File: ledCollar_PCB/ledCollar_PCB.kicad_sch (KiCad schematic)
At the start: 27 parts, among them J1 PWR, J2 SWD, J3 APA102, J4 MAX9814 Breakout, Q1 AO3400A, SW1 SW_Push, U1 AP2112K-3.3, U2 STM32F103C8Tx, U3 NRF24L01_Breakout, U4 MAX9814

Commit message: some layout tweaks, nothing major
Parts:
- added C10, C13: 100n, Capacitor_SMD:C_0603_1608Metric, symbol Device:C
- added C11: 10n, Capacitor_SMD:C_0603_1608Metric, symbol Device:C
- added C12: 2n2, Capacitor_SMD:C_0603_1608Metric, symbol Device:C
- added U5: MPU-6050, Sensor_Motion:InvenSense_QFN-24_4x4mm_P0.5mm, symbol Sensor_Motion:MPU-6050
- J4: footprint Connector_PinSocket_2.54mm:PinSocket_1x05_P2.54mm_Vertical -> (none)
- MK1: footprint Connector_PinHeader_2.54mm:PinHeader_1x02_P2.54mm_Vertical -> LeoDJ:Microphone_9.5mm
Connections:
- net +3V3: now also C10.1, C11.1, U5.13 (VDD), U5.8 (VDDIO), U5.9 (AD0)
- net GND: now also C10.2, C11.2, C12.2, C13.2, U5.1 (CLKIN), U5.11 (FSYNC), U5.18 (GND)
- net MICBIAS: now reaches R6.2, R7.1, U4.13 (MICBIAS)
- net MPU_IRQ: now reaches U2.20 (PB2)
- net MPU_IRQ: now also U5.12 (INT)
- net SCL: now reaches U2.21 (PB10)
- net SCL: now also U5.23 (SCL)
- net SDA: now reaches U2.22 (PB11)
- net SDA: now also U5.24 (SDA)
- net MICIN: now reaches C5.2, U4.8 (MICIN)
- new net: C13.1, U5.10 (REGOUT)
- new net: C12.1, U5.20 (CPOUT)

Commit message: *layouting sounds*
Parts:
- removed J1: PWR, symbol Connector_Generic:Conn_01x02
- removed J4: MAX9814 Breakout, symbol Connector_Generic:Conn_01x05
- added J1: PWR+, TestPoint:TestPoint_Pad_1.5x1.5mm, symbol Connector_Generic:Conn_01x01
- added J2: PWR-, TestPoint:TestPoint_Pad_1.5x1.5mm, symbol Connector_Generic:Conn_01x01
- added R8, R9: 10k, Resistor_SMD:R_0603_1608Metric, symbol Device:R
- renumbered J2 to J6
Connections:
- net +3V3: now also R8.1, R9.1
- net GND: now also J2.1 (Pin_1)
- net SCL: now also U2.45 (PB8), R8.2; no longer U2.21 (PB10)
- net SDA: now also U2.46 (PB9), R9.2; no longer U2.22 (PB11)
- net VCC: now also J1.1 (Pin_1)
- net LED_GND: now reaches J3.1 (Pin_1), Q1.3 (D)

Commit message: add light sensor
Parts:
- added Q2: Q_Photo_NPN, LED_SMD:LED_0805_2012Metric_Castellated, symbol Device:Q_Photo_NPN
- added R10: 10k, Resistor_SMD:R_0603_1608Metric, symbol Device:R
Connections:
- net +3V3: now also Q2.1 (C)
- net GND: now also R10.2
- net MIC_OUT: now also U2.17 (PA7); no longer U2.18 (PB0)
- new net LIGHT_SENSE: Q2.2 (E), R10.1, U2.18 (PB0)
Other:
- note added: "Senba SMD0805-20 Collector has same marking like SMD LED cathode (arrow pointing to it)"

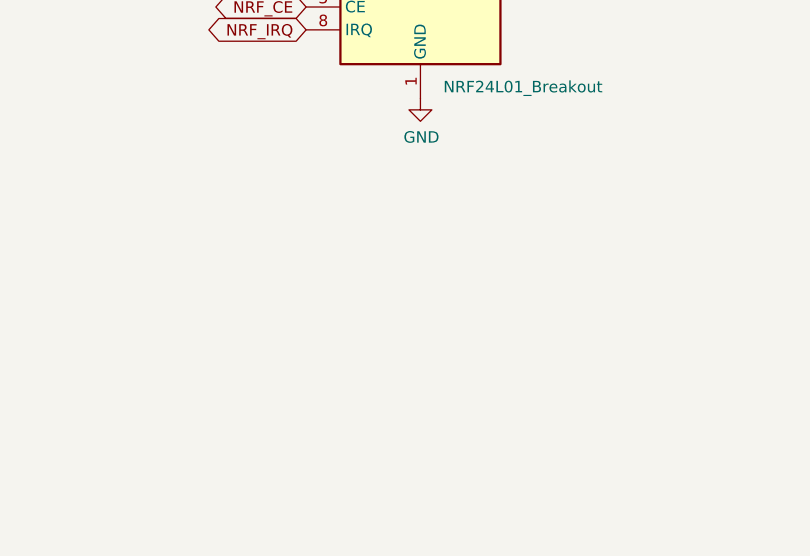
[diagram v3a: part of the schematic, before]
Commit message: add alternate NRF footprint
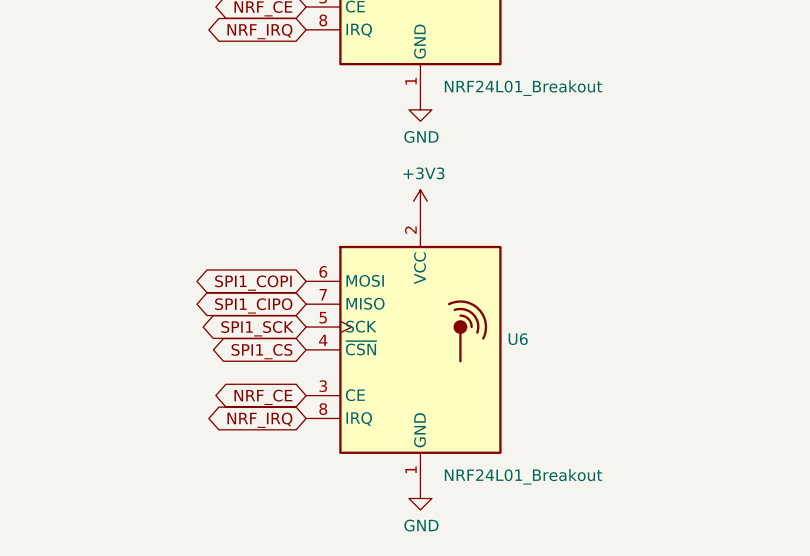
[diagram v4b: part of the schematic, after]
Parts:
- added U6: NRF24L01_Breakout, LeoDJ:NRF24L01_SMD_PadsOnly, symbol RF:NRF24L01_Breakout
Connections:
- net +3V3: now also U6.2 (VCC)
- net GND: now also U6.1 (GND)
- net NRF_CE: now also U6.3 (CE)
- net NRF_IRQ: now also U6.8 (IRQ)
- net SPI1_CIPO: now also U6.7 (MISO)
- net SPI1_COPI: now also U6.6 (MOSI)
- net SPI1_CS: now also U6.4 (~CSN)
- net SPI1_SCK: now also U6.5 (SCK)
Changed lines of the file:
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@@
+    (effects (font (size 1.27 1.27)) (justify right))
+  )
+  (global_label "SPI1_COPI" (shape bidirectional) (at 229.87 185.42 180)
+    (effects (font (size 1.27 1.27)) (justify right))
+  )
+  (global_label "SPI1_CIPO" (shape bidirectional) (at 229.87 187.96 180)
+    (effects (font (size 1.27 1.27)) (justify right))
+  )
+  (global_label "SPI1_SCK" (shape bidirectional) (at 229.87 190.5 180)
+    (effects (font (size 1.27 1.27)) (justify right))
+  )
+  (global_label "SPI1_CS" (shape bidirectional) (at 229.87 193.04 180)
+    (effects (font (size 1.27 1.27)) (justify right))
+  )
+  (global_label "NRF_CE" (shape bidirectional) (at 229.87 198.12 180)
+    (effects (font (size 1.27 1.27)) (justify right))
+  )
+  (global_label "NRF_IRQ" (shape bidirectional) (at 229.87 200.66 180)
     (effects (font (size 1.27 1.27)) (justify right))
   )
@@
     )
   )
+  (symbol (lib_id "power:+3V3") (at 242.57 177.8 0)
+    (in_bom yes) (on_board yes)
+    (property "Reference" "#PWR0142" (id 0) (at 242.57 181.61 0)
+      (effects (font (size 1.27 1.27)) hide)
+    )
+    (property "Value" "+3V3" (id 1) (at 242.9383 173.4756 0))
+    (property "Footprint" "" (id 2) (at 242.57 177.8 0)
+      (effects (font (size 1.27 1.27)) hide)
+    )
+    (property "Datasheet" "" (id 3) (at 242.57 177.8 0)
+      (effects (font (size 1.27 1.27)) hide)
+    )
+  )
   (symbol (lib_id "power:+3V3") (at 256.54 134.62 0)
     (in_bom yes) (on_board yes)
@@
     )
     (property "Datasheet" "" (id 3) (at 242.57 165.1 0)
+      (effects (font (size 1.27 1.27)) hide)
+    )
+  )
+  (symbol (lib_id "power:GND") (at 242.57 208.28 0)
+    (in_bom yes) (on_board yes)
+    (property "Reference" "#PWR0143" (id 0) (at 242.57 214.63 0)
+      (effects (font (size 1.27 1.27)) hide)
+    )
+    (property "Value" "GND" (id 1) (at 242.6843 212.6044 0))
+    (property "Footprint" "" (id 2) (at 242.57 208.28 0)
+      (effects (font (size 1.27 1.27)) hide)
+    )
+    (property "Datasheet" "" (id 3) (at 242.57 208.28 0)
       (effects (font (size 1.27 1.27)) hide)
     )
@@
     )
     (property "Datasheet" "http://www.nordicsemi.com/eng/content/download/2730/34105/file/nRF24L01_Product_Specification_v2_0.pdf" (id 3) (at 242.57 152.4 0)
+      (effects (font (size 1.27 1.27)) hide)
+    )
+  )
+  (symbol (lib_id "RF:NRF24L01_Breakout") (at 242.57 193.04 0)
+    (in_bom yes) (on_board yes)
+    (property "Reference" "U6" (id 0) (at 252.2221 191.8906 0)
+      (effects (font (size 1.27 1.27)) (justify left))
+    )
+    (property "Value" "NRF24L01_Breakout" (id 1) (at 245.11 207.01 0)
+      (effects (font (size 1.27 1.27)) (justify left))
+    )
+    (property "Footprint" "LeoDJ:NRF24L01_SMD_PadsOnly" (id 2) (at 246.38 177.8 0)
+      (effects (font (size 1.27 1.27) italic) (justify left) hide)
+    )
+    (property "Datasheet" "http://www.nordicsemi.com/eng/content/download/2730/34105/file/nRF24L01_Product_Specification_v2_0.pdf" (id 3) (at 242.57 195.58 0)
       (effects (font (size 1.27 1.27)) hide)
     )
@@
       (reference "#PWR0141") (unit 1)
     )
+    (path "/8e883048-16df-4df7-8725-260d2556d700"
+      (reference "#PWR0142") (unit 1)
+    )
+    (path "/e1abf090-d70f-4ab4-accf-1fb2fae9b3e2"
+      (reference "#PWR0143") (unit 1)
+    )
     (path "/bbebd2f4-9685-40e0-9522-a5708083ab20"
       (reference "C1") (unit 1)
@@
       (reference "U5") (unit 1)
     )
-  )
+    (path "/71aeef5b-e0de-4f1c-944d-86037faa92ea"
+      (reference "U6") (unit 1)
+    )
+  )

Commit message: PCB finishing touches
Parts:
- added GR1: QR Code, LeoDJ:QR_Code_LEDCollar, symbol LeoDJ:GenericGraphic
- added GR2: Logo_Open_Hardware_Small, Symbol:OSHW-Logo2_7.3x6mm_SilkScreen, symbol Graphic:Logo_Open_Hardware_Small
- J3: footprint Connector_Harwin:Harwin_M20-89004xx_1x04_P2.54mm_Horizontal -> LeoDJ:APA102_SolderPads
- Q2: value Q_Photo_NPN -> Senba SMD0805-20
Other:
- note added: "Alternative Footprint"
- note added: "Collector has same marking like SMD LED cathode (arrow pointing to it)"
- note removed: "Senba SMD0805-20 Collector has same marking like SMD LED cathode (arrow pointing to it)"
- moved on the sheet: C1, C10, C11, C12, C13, C2, C3, C4, C5, C6, C7, C8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

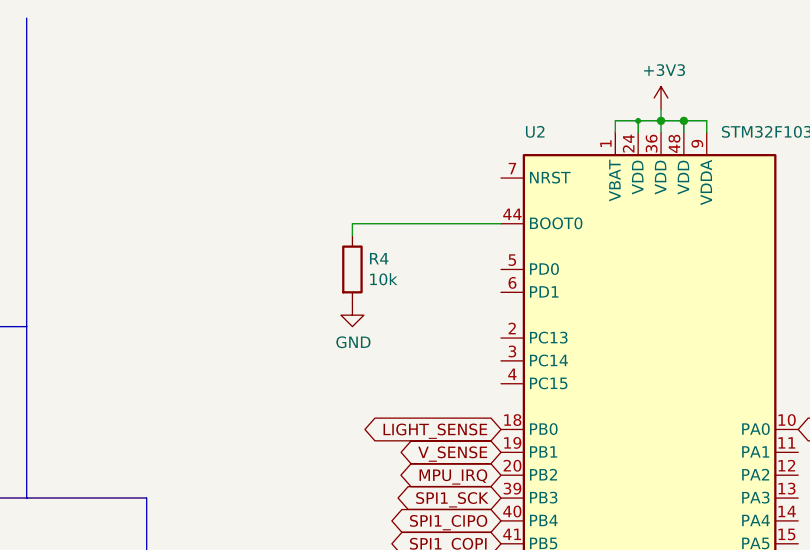
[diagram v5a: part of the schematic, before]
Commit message: add cap to STM32 reset pin
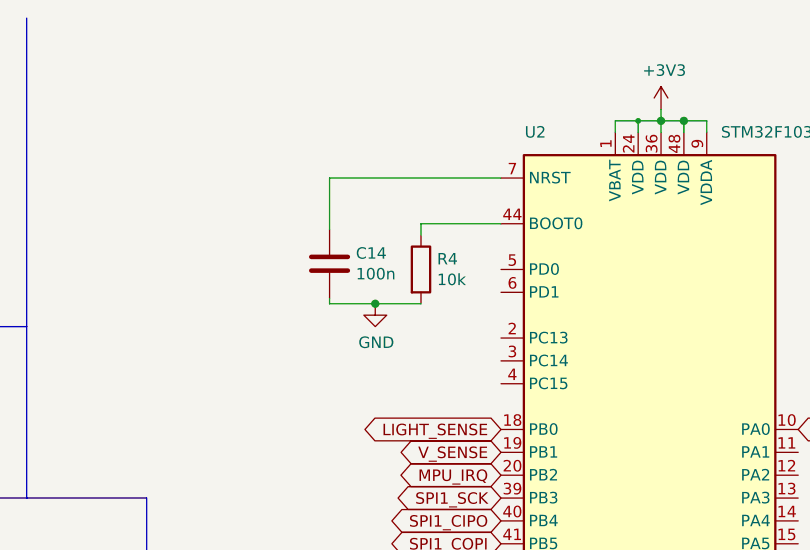
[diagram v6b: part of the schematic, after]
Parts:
- added C14: 100n, Capacitor_SMD:C_0603_1608Metric, symbol Device:C
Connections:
- net GND: now also C14.1
- net at U2.7 (NRST): now also C14.2
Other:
- moved on the sheet: R4
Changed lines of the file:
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@@
   (junction (at 77.47 89.535) (diameter 0) (color 0 0 0 0))
   (junction (at 102.87 171.45) (diameter 0) (color 0 0 0 0))
+  (junction (at 135.89 43.815) (diameter 0) (color 0 0 0 0))
   (junction (at 165.1 23.495) (diameter 0.635) (color 0 0 0 0))
   (junction (at 165.1 100.965) (diameter 0) (color 0 0 0 0))
@@
     (stroke (width 0) (type solid) (color 0 0 0 0))
   )
-  (wire (pts (xy 133.35 34.925) (xy 133.35 36.195))
-    (stroke (width 0) (type solid) (color 0 0 0 0))
-  )
-  (wire (pts (xy 149.86 34.925) (xy 133.35 34.925))
+  (wire (pts (xy 130.81 29.845) (xy 130.81 35.56))
+    (stroke (width 0) (type solid) (color 0 0 0 0))
+  )
+  (wire (pts (xy 130.81 43.815) (xy 130.81 43.18))
+    (stroke (width 0) (type solid) (color 0 0 0 0))
+  )
+  (wire (pts (xy 135.89 43.815) (xy 130.81 43.815))
+    (stroke (width 0) (type solid) (color 0 0 0 0))
+  )
+  (wire (pts (xy 135.89 43.815) (xy 140.97 43.815))
+    (stroke (width 0) (type solid) (color 0 0 0 0))
+  )
+  (wire (pts (xy 140.97 34.925) (xy 140.97 36.195))
+    (stroke (width 0) (type solid) (color 0 0 0 0))
+  )
+  (wire (pts (xy 149.86 29.845) (xy 130.81 29.845))
+    (stroke (width 0) (type solid) (color 0 0 0 0))
+  )
+  (wire (pts (xy 149.86 34.925) (xy 140.97 34.925))
     (stroke (width 0) (type solid) (color 0 0 0 0))
   )
@@
     )
   )
-  (symbol (lib_id "power:GND") (at 133.35 43.815 0)
-    (in_bom yes) (on_board yes)
-    (property "Reference" "#PWR0121" (id 0) (at 133.35 50.165 0)
-      (effects (font (size 1.27 1.27)) hide)
-    )
-    (property "Value" "GND" (id 1) (at 133.4643 48.1394 0))
-    (property "Footprint" "" (id 2) (at 133.35 43.815 0)
-      (effects (font (size 1.27 1.27)) hide)
-    )
-    (property "Datasheet" "" (id 3) (at 133.35 43.815 0)
+  (symbol (lib_id "power:GND") (at 135.89 43.815 0)
+    (in_bom yes) (on_board yes)
+    (property "Reference" "#PWR0121" (id 0) (at 135.89 50.165 0)
+      (effects (font (size 1.27 1.27)) hide)
+    )
+    (property "Value" "GND" (id 1) (at 136.0043 48.1394 0))
+    (property "Footprint" "" (id 2) (at 135.89 43.815 0)
+      (effects (font (size 1.27 1.27)) hide)
+    )
+    (property "Datasheet" "" (id 3) (at 135.89 43.815 0)
       (effects (font (size 1.27 1.27)) hide)
     )
@@
     )
   )
-  (symbol (lib_id "Device:R") (at 133.35 40.005 0)
-    (in_bom yes) (on_board yes)
-    (property "Reference" "R4" (id 0) (at 135.1281 38.8556 0)
-      (effects (font (size 1.27 1.27)) (justify left))
-    )
-    (property "Value" "10k" (id 1) (at 135.128 41.154 0)
-      (effects (font (size 1.27 1.27)) (justify left))
-    )
-    (property "Footprint" "Resistor_SMD:R_0603_1608Metric" (id 2) (at 131.572 40.005 90)
-      (effects (font (size 1.27 1.27)) hide)
-    )
-    (property "Datasheet" "~" (id 3) (at 133.35 40.005 0)
+  (symbol (lib_id "Device:R") (at 140.97 40.005 0)
+    (in_bom yes) (on_board yes)
+    (property "Reference" "R4" (id 0) (at 142.7481 38.8556 0)
+      (effects (font (size 1.27 1.27)) (justify left))
+    )
+    (property "Value" "10k" (id 1) (at 142.748 41.154 0)
+      (effects (font (size 1.27 1.27)) (justify left))
+    )
+    (property "Footprint" "Resistor_SMD:R_0603_1608Metric" (id 2) (at 139.192 40.005 90)
+      (effects (font (size 1.27 1.27)) hide)
+    )
+    (property "Datasheet" "~" (id 3) (at 140.97 40.005 0)
       (effects (font (size 1.27 1.27)) hide)
     )
@@
     )
     (property "Datasheet" "~" (id 3) (at 130.175 157.48 0)
+      (effects (font (size 1.27 1.27)) hide)
+    )
+  )
+  (symbol (lib_id "Device:C") (at 130.81 39.37 180)
+    (in_bom yes) (on_board yes)
+    (property "Reference" "C14" (id 0) (at 133.7311 38.2206 0)
+      (effects (font (size 1.27 1.27)) (justify right))
+    )
+    (property "Value" "100n" (id 1) (at 133.731 40.519 0)
+      (effects (font (size 1.27 1.27)) (justify right))
+    )
+    (property "Footprint" "Capacitor_SMD:C_0603_1608Metric" (id 2) (at 129.8448 35.56 0)
+      (effects (font (size 1.27 1.27)) hide)
+    )
+    (property "Datasheet" "~" (id 3) (at 130.81 39.37 0)
       (effects (font (size 1.27 1.27)) hide)
     )
@@
       (reference "C13") (unit 1)
     )
+    (path "/1c71a604-d29a-44db-b225-1ffe77f022ad"
+      (reference "C14") (unit 1)
+    )
     (path "/1e18a7f3-1069-4097-b796-5dffa9df0099"
